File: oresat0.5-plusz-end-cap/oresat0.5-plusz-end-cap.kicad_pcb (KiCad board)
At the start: 2 copper layers, 105.6 x 105.6 mm, 44 parts, among them J2 U.FL-R-SMA, U1 LTC4305

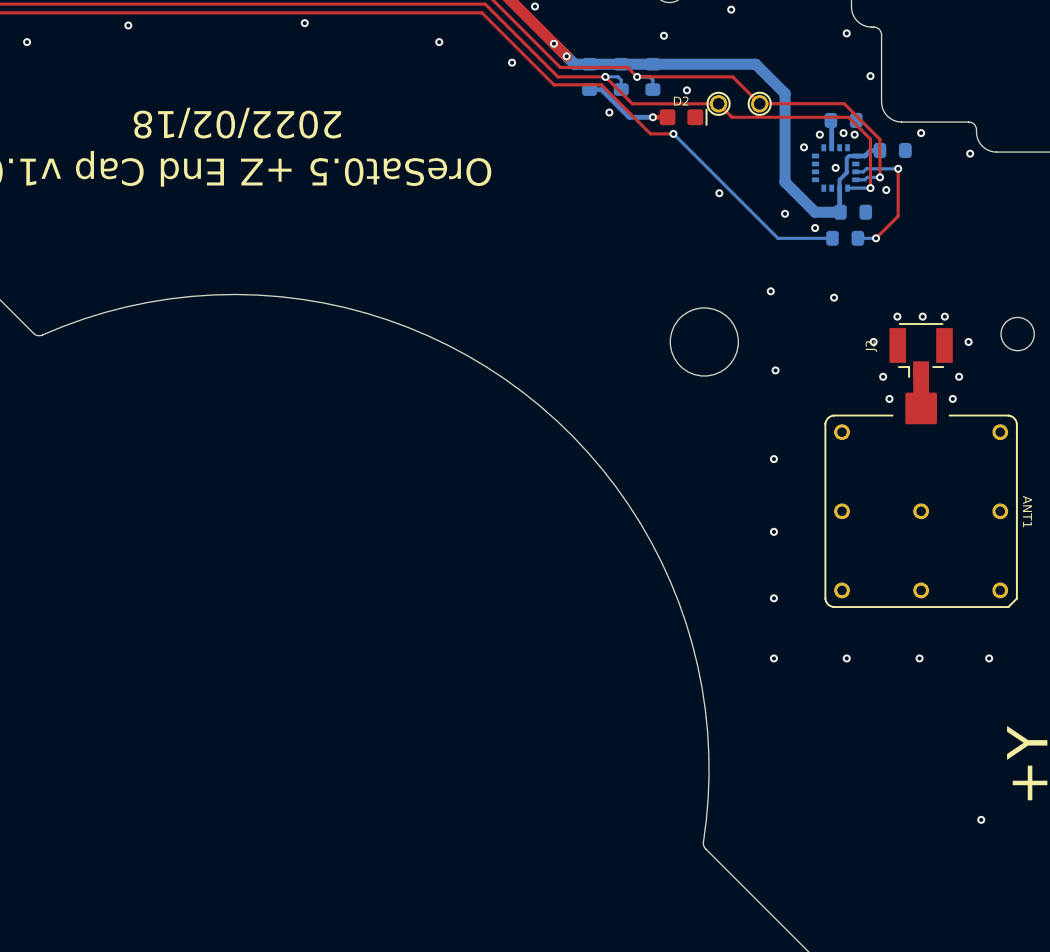
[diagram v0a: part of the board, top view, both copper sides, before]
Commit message: Added white silkscreen square for board number! Super critical! :)
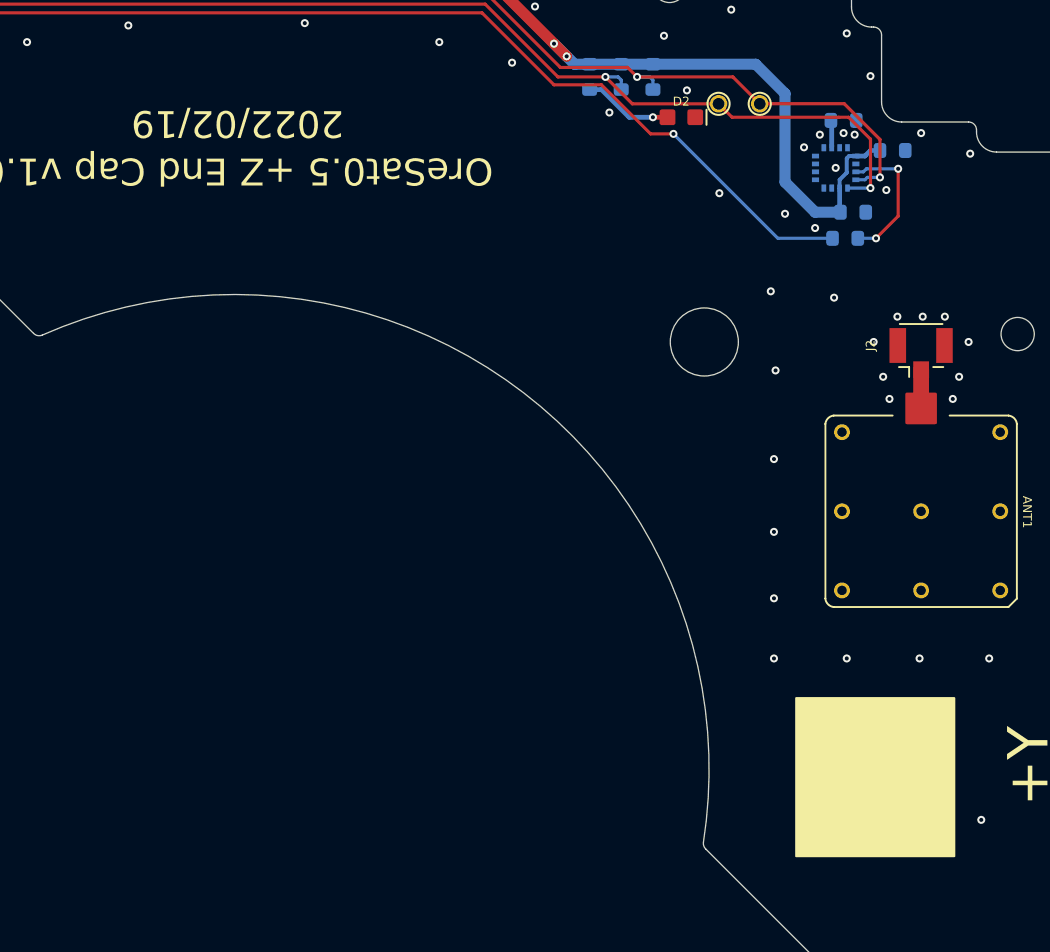
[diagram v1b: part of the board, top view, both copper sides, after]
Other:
- board text added: "2022/02/19"
- board text removed: "2022/02/18"
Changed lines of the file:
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@@
       (net 17 "Net-(R12-Pad2)") (pinfunction "2") (pintype "passive") (solder_mask_margin 0.0635))
   )
+  (gr_rect (start 184 100.5) (end 194 110.5) (layer "F.SilkS") (width 0.12) (fill solid))
   (gr_rect (start 107.7 57.7) (end 189.3 52.3) (layer "B.Mask") (width 0.2) (fill solid))
   (gr_rect (start 107.7 157.7) (end 189.3 152.3) (layer "B.Mask") (width 0.2) (fill solid))
@@
     (effects (font (size 2.55 2.55) (thickness 0.45)))
   )
-  (gr_text "2022/02/18" (at 148.7 64.2 180) (layer "F.SilkS")
+  (gr_text "2022/02/19" (at 148.7 64.2 180) (layer "F.SilkS")
     (effects (font (size 1.7 1.7) (thickness 0.3)))
   )

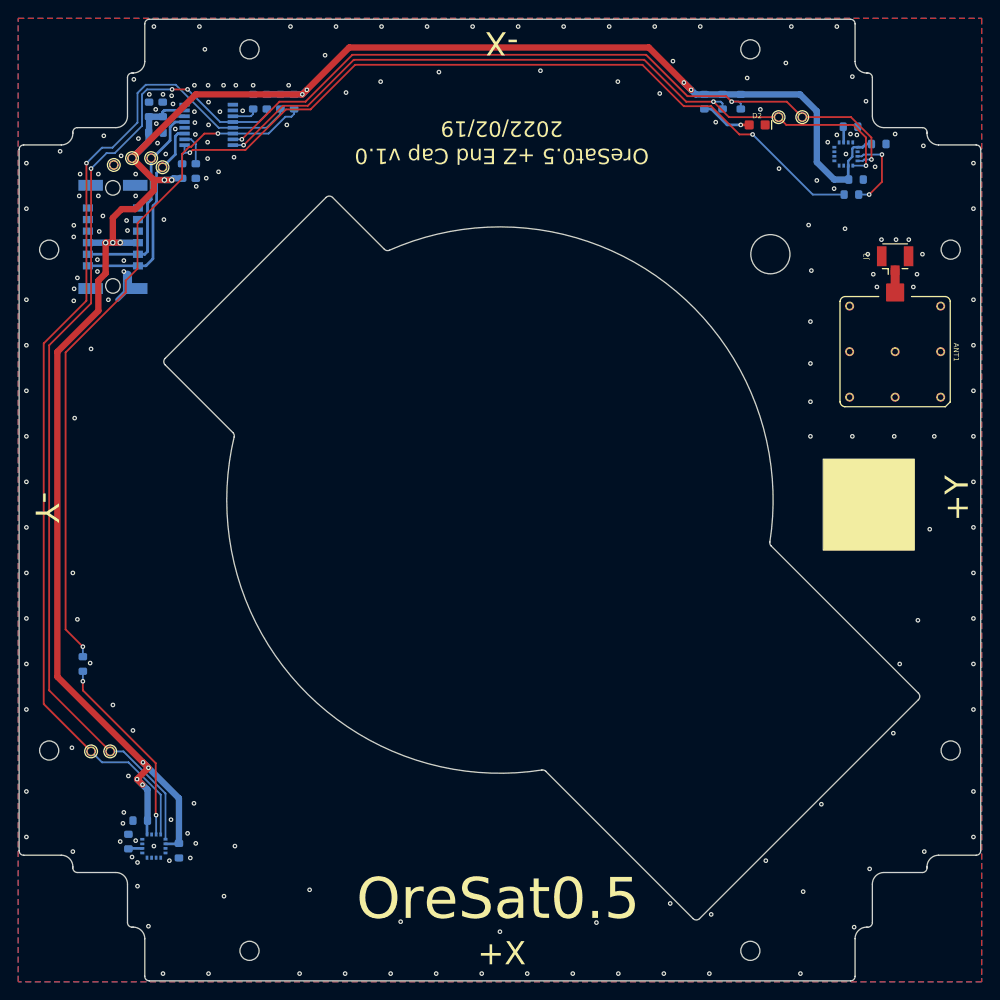
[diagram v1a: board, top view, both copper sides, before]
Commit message: Updated end caps
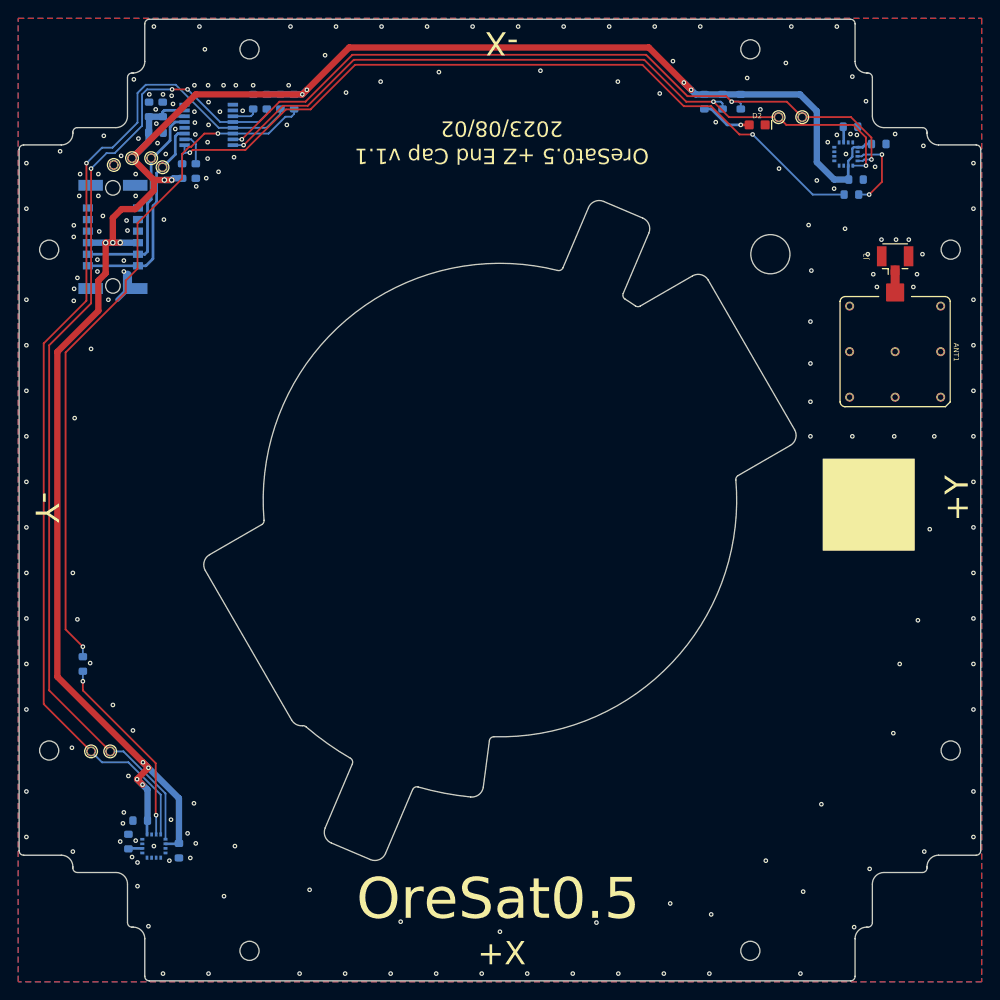
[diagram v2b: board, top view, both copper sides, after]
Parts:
- J1: footprint oresat0-plusz-end-cap:HARWIN-M55-70X1242R -> oresat0.5-plusz-end-cap:HARWIN-M55-70X1242R
- TP1, TP2, TP3, TP4, TP5, TP6, TP7, TP8: footprint oresat0-plusz-end-cap:1X01 -> oresat-misc:TestPoint-0.75mm-th
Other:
- outline, holes or cut-outs redrawn
- board text added: "2023/08/02"
- board text added: "OreSat0.5 +Z End Cap v1.1"
- board text removed: "2022/02/19"
- board text removed: "OreSat0.5 +Z End Cap v1.0"

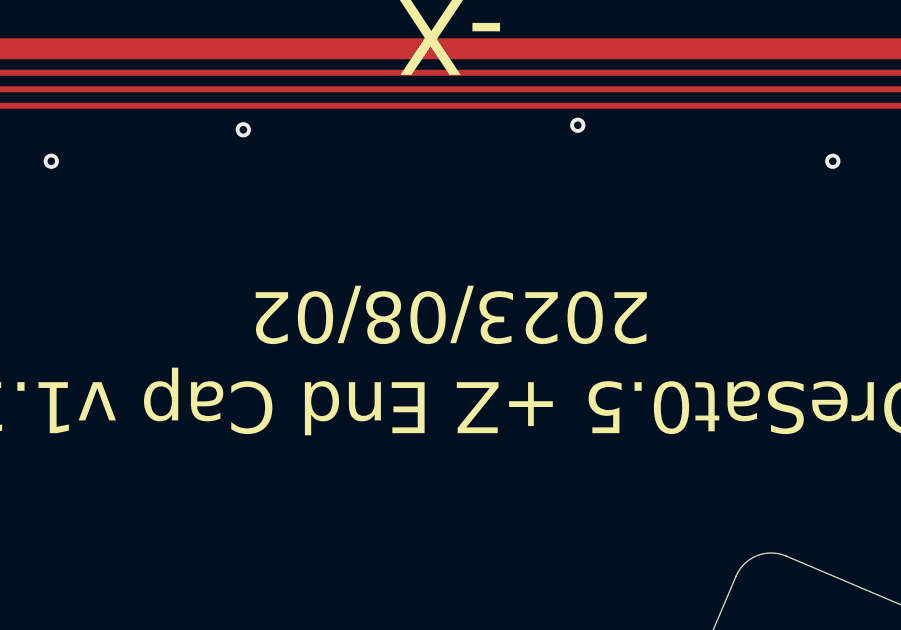
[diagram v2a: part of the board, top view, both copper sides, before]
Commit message: Updated mounting holes
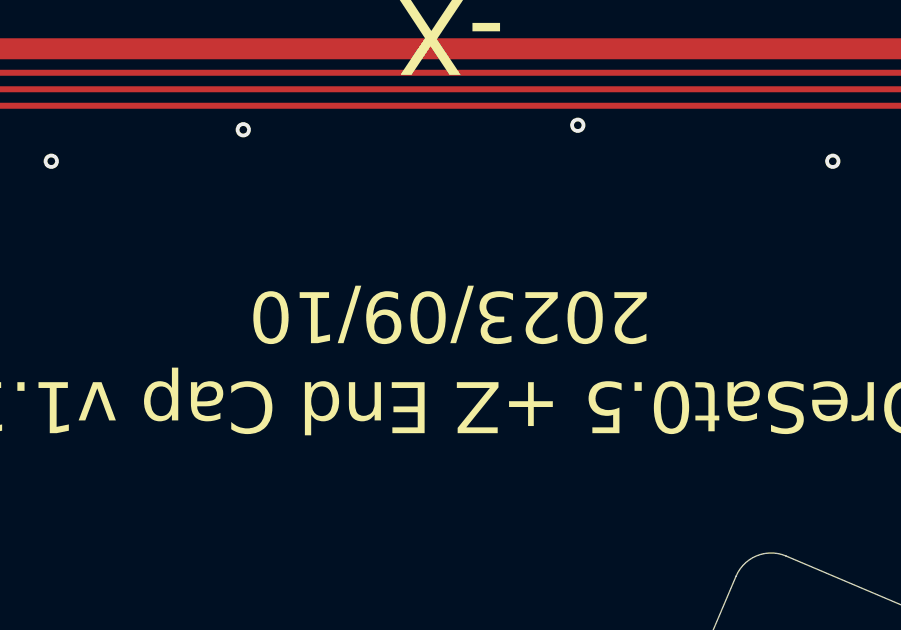
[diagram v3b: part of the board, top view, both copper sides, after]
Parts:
- U2, U3: value (none) -> MMC5883MA
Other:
- board text added: "2023/09/10"
- board text removed: "2023/08/02"
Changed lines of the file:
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@@
     (property "Sheetfile" "oresat0.5-plusz-end-cap.kicad_sch")
     (property "Sheetname" "")
-    (property "Value" "")
+    (property "Value" "MMC5883MA")
     (fp_text reference "U3" (at -2.3 0.3) (layer "B.SilkS")
         (effects (font (size 0.56 0.56) (thickness 0.12)) (justify right mirror))
@@
       (net 1 "3.3V") (pinfunction "VDD") (pintype "power_in") (solder_mask_margin 0.0635))
     (pad "3" smd rect (at -0.25 1.275 90) (size 0.3 0.45) (layers "B.Cu" "B.Paste" "B.Mask")
-      (solder_mask_margin 0.0635))
+      (pinfunction "NC") (pintype "no_connect") (solder_mask_margin 0.0635))
     (pad "4" smd rect (at -0.75 1.275 90) (size 0.3 0.45) (layers "B.Cu" "B.Paste" "B.Mask")
-      (solder_mask_margin 0.0635))
+      (pinfunction "NC") (pintype "no_connect") (solder_mask_margin 0.0635))
     (pad "5" smd rect (at -1.275 0.75) (size 0.3 0.45) (layers "B.Cu" "B.Paste" "B.Mask")
-      (solder_mask_margin 0.0635))
+      (pinfunction "NC") (pintype "no_connect") (solder_mask_margin 0.0635))
     (pad "6" smd rect (at -1.275 0.25) (size 0.3 0.45) (layers "B.Cu" "B.Paste" "B.Mask")
-      (solder_mask_margin 0.0635))
+      (pinfunction "NC") (pintype "no_connect") (solder_mask_margin 0.0635))
     (pad "7" smd rect (at -1.275 -0.25) (size 0.3 0.45) (layers "B.Cu" "B.Paste" "B.Mask")
-      (solder_mask_margin 0.0635))
+      (pinfunction "NC") (pintype "no_connect") (solder_mask_margin 0.0635))
     (pad "8" smd rect (at -1.275 -0.75) (size 0.3 0.45) (layers "B.Cu" "B.Paste" "B.Mask")
-      (solder_mask_margin 0.0635))
+      (pinfunction "NC") (pintype "no_connect") (solder_mask_margin 0.0635))
     (pad "9" smd rect (at -0.75 -1.275 270) (size 0.3 0.45) (layers "B.Cu" "B.Paste" "B.Mask")
       (net 2 "GND") (pinfunction "GND") (pintype "power_in") (solder_mask_margin 0.0635))
@@
       (net 2 "GND") (pinfunction "GND") (pintype "power_in") (solder_mask_margin 0.0635))
     (pad "12" smd rect (at 0.75 -1.275 270) (size 0.3 0.45) (layers "B.Cu" "B.Paste" "B.Mask")
-      (solder_mask_margin 0.0635))
+      (pinfunction "NC") (pintype "no_connect") (solder_mask_margin 0.0635))
     (pad "13" smd rect (at 1.275 -0.75 180) (size 0.3 0.45) (layers "B.Cu" "B.Paste" "B.Mask")
       (net 1 "3.3V") (pinfunction "VDDIO") (pintype "power_in") (solder_mask_margin 0.0635))
     (pad "14" smd rect (at 1.275 -0.25 180) (size 0.3 0.45) (layers "B.Cu" "B.Paste" "B.Mask")
-      (solder_mask_margin 0.0635))
+      (pinfunction "NC") (pintype "no_connect") (solder_mask_margin 0.0635))
     (pad "15" smd rect (at 1.275 0.25 180) (size 0.3 0.45) (layers "B.Cu" "B.Paste" "B.Mask")
       (net 21 "Net-(U3-INT)") (pinfunction "INT") (pintype "output") (solder_mask_margin 0.0635))
@@
     (property "Sheetfile" "oresat0.5-plusz-end-cap.kicad_sch")
     (property "Sheetname" "")
-    (property "Value" "")
+    (property "Value" "MMC5883MA")
     (fp_text reference "U2" (at -1.8 0.3) (layer "B.SilkS")
         (effects (font (size 0.56 0.56) (thickness 0.12)) (justify left mirror))
@@
       (net 1 "3.3V") (pinfunction "VDD") (pintype "power_in") (solder_mask_margin 0.0635))
     (pad "3" smd rect (at -0.25 1.275) (size 0.3 0.45) (layers "B.Cu" "B.Paste" "B.Mask")
-      (solder_mask_margin 0.0635))
+      (pinfunction "NC") (pintype "no_connect") (solder_mask_margin 0.0635))
     (pad "4" smd rect (at -0.75 1.275) (size 0.3 0.45) (layers "B.Cu" "B.Paste" "B.Mask")
-      (solder_mask_margin 0.0635))
+      (pinfunction "NC") (pintype "no_connect") (solder_mask_margin 0.0635))
     (pad "5" smd rect (at -1.275 0.75 270) (size 0.3 0.45) (layers "B.Cu" "B.Paste" "B.Mask")
-      (solder_mask_margin 0.0635))
+      (pinfunction "NC") (pintype "no_connect") (solder_mask_margin 0.0635))
     (pad "6" smd rect (at -1.275 0.25 270) (size 0.3 0.45) (layers "B.Cu" "B.Paste" "B.Mask")
-      (solder_mask_margin 0.0635))
+      (pinfunction "NC") (pintype "no_connect") (solder_mask_margin 0.0635))
     (pad "7" smd rect (at -1.275 -0.25 270) (size 0.3 0.45) (layers "B.Cu" "B.Paste" "B.Mask")
-      (solder_mask_margin 0.0635))
+      (pinfunction "NC") (pintype "no_connect") (solder_mask_margin 0.0635))
     (pad "8" smd rect (at -1.275 -0.75 270) (size 0.3 0.45) (layers "B.Cu" "B.Paste" "B.Mask")
-      (solder_mask_margin 0.0635))
+      (pinfunction "NC") (pintype "no_connect") (solder_mask_margin 0.0635))
     (pad "9" smd rect (at -0.75 -1.275 180) (size 0.3 0.45) (layers "B.Cu" "B.Paste" "B.Mask")
       (net 2 "GND") (pinfunction "GND") (pintype "power_in") (solder_mask_margin 0.0635))
@@
       (net 2 "GND") (pinfunction "GND") (pintype "power_in") (solder_mask_margin 0.0635))
     (pad "12" smd rect (at 0.75 -1.275 180) (size 0.3 0.45) (layers "B.Cu" "B.Paste" "B.Mask")
-      (solder_mask_margin 0.0635))
+      (pinfunction "NC") (pintype "no_connect") (solder_mask_margin 0.0635))
     (pad "13" smd rect (at 1.275 -0.75 90) (size 0.3 0.45) (layers "B.Cu" "B.Paste" "B.Mask")
       (net 1 "3.3V") (pinfunction "VDDIO") (pintype "power_in") (solder_mask_margin 0.0635))
     (pad "14" smd rect (at 1.275 -0.25 90) (size 0.3 0.45) (layers "B.Cu" "B.Paste" "B.Mask")
-      (solder_mask_margin 0.0635))
+      (pinfunction "NC") (pintype "no_connect") (solder_mask_margin 0.0635))
     (pad "15" smd rect (at 1.275 0.25 90) (size 0.3 0.45) (layers "B.Cu" "B.Paste" "B.Mask")
       (net 23 "Net-(U2-INT)") (pinfunction "INT") (pintype "output") (solder_mask_margin 0.0635))
@@
     (effects (font (size 2.55 2.55) (thickness 0.45)))
   )
-  (gr_text "2023/08/02" (at 148.7 64.2 180) (layer "F.SilkS")
+  (gr_text "2023/09/10" (at 148.7 64.2 180) (layer "F.SilkS")
     (effects (font (size 1.7 1.7) (thickness 0.3)))
   )
